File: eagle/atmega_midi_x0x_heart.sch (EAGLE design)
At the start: 39 parts, among them J11_VCF_CUTOFF 22-23-2021, U1 ATMEGA328P_PDIP, U2 TLV2372IP

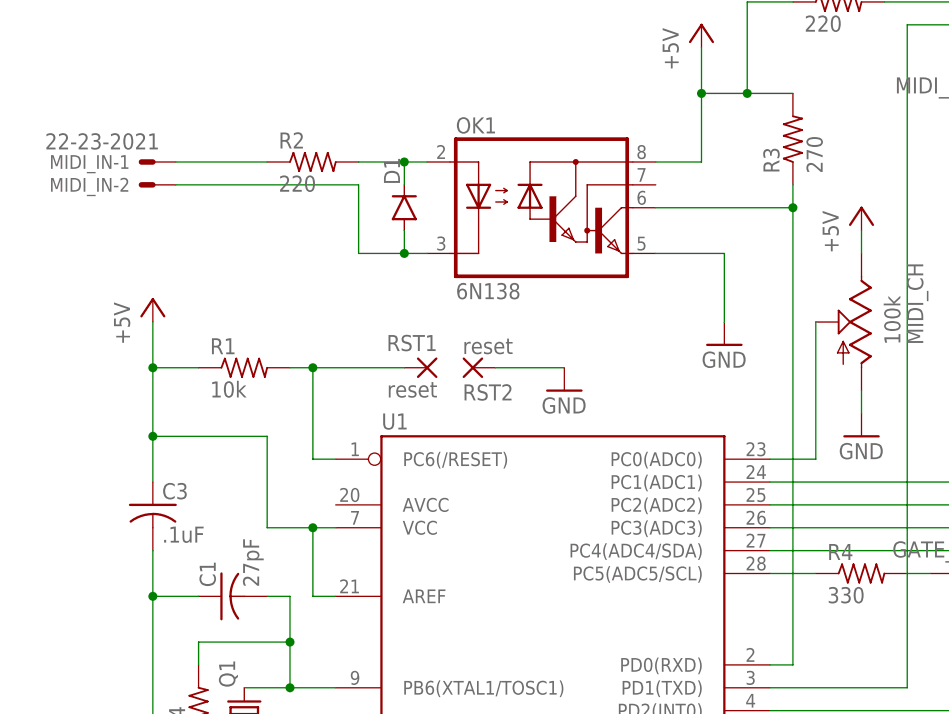
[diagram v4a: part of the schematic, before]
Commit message: initial layout for res control version
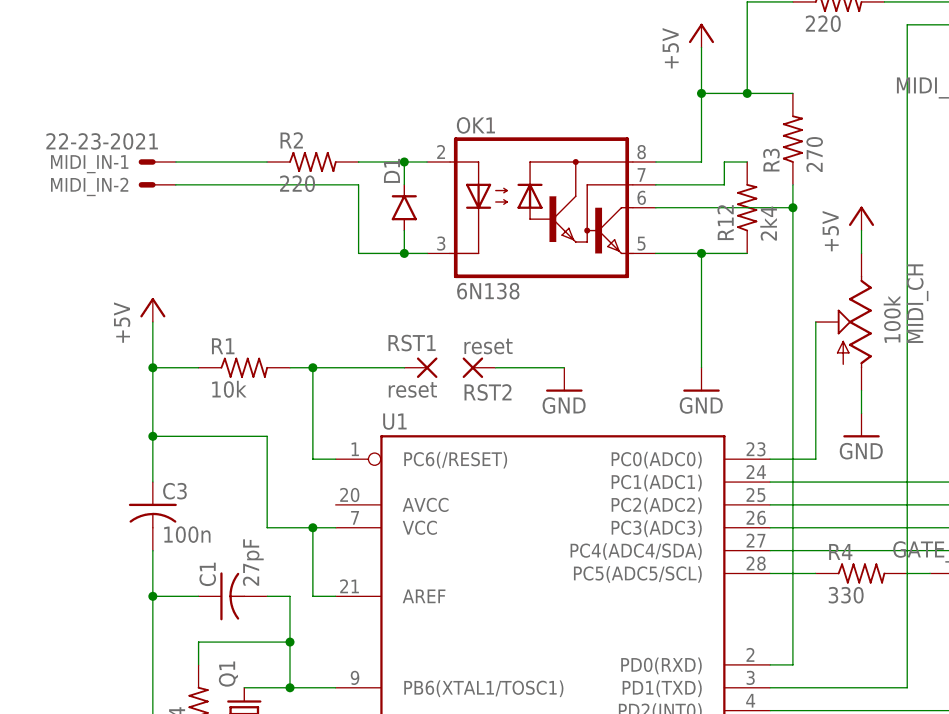
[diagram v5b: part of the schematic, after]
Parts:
- added R12: 2k4, rcl:R-US_0207/10
- C3: value .1uF -> 100n
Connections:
- new net N$44: OK1.VB, R12.2
- net GND: now also R12.1
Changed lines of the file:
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@@
 <part name="R1" library="rcl" deviceset="R-US_" device="0207/10" value="10k"/>
 <part name="OK1" library="optocoupler" deviceset="6N138" device=""/>
-<part name="C3" library="rcl" deviceset="C-US" device="050-024X044" value=".1uF"/>
+<part name="C3" library="rcl" deviceset="C-US" device="050-024X044" value="100n"/>
 <part name="D1" library="SparkFun-DiscreteSemi" deviceset="DIODE" device="1N4148"/>
 <part name="R2" library="rcl" deviceset="R-US_" device="0207/10" value="220"/>
@@
 <part name="MIDI_OUT_THRU" library="con-lstb" deviceset="MA03-1" device=""/>
 <part name="GND15" library="supply1" deviceset="GND" device=""/>
+<part name="R12" library="rcl" deviceset="R-US_" device="0207/10" value="2k4"/>
 </parts>
 <sheets>
@@
 <instance part="GND1" gate="1" x="-25.4" y="10.16"/>
 <instance part="GND2" gate="1" x="20.32" y="81.28"/>
-<instance part="GND3" gate="1" x="38.1" y="86.36"/>
+<instance part="GND3" gate="1" x="35.56" y="81.28"/>
 <instance part="GND4" gate="1" x="73.66" y="78.74"/>
 <instance part="GND5" gate="1" x="53.34" y="76.2"/>
@@
 <instance part="MIDI_OUT_THRU" gate="G$1" x="73.66" y="121.92" rot="R180"/>
 <instance part="GND15" gate="1" x="66.04" y="111.76"/>
+<instance part="R12" gate="G$1" x="40.64" y="101.6" rot="R90"/>
 </instances>
 <busses>
@@
 </segment>
 <segment>
-<wire x1="38.1" y1="96.52" x2="38.1" y2="88.9" width="0.1524" layer="91"/>
+<wire x1="35.56" y1="96.52" x2="35.56" y2="83.82" width="0.1524" layer="91"/>
 <pinref part="OK1" gate="G$1" pin="GND"/>
-<wire x1="30.48" y1="96.52" x2="38.1" y2="96.52" width="0.1524" layer="91"/>
+<wire x1="30.48" y1="96.52" x2="35.56" y2="96.52" width="0.1524" layer="91"/>
 <pinref part="GND3" gate="1" pin="GND"/>
+<pinref part="R12" gate="G$1" pin="1"/>
+<wire x1="40.64" y1="96.52" x2="35.56" y2="96.52" width="0.1524" layer="91"/>
+<junction x="35.56" y="96.52"/>
 </segment>
 <segment>
@@
 </segment>
 </net>
+<net name="N$44" class="0">
+<segment>
+<pinref part="OK1" gate="G$1" pin="VB"/>
+<wire x1="30.48" y1="104.14" x2="38.1" y2="104.14" width="0.1524" layer="91"/>
+<wire x1="38.1" y1="104.14" x2="38.1" y2="106.68" width="0.1524" layer="91"/>
+<pinref part="R12" gate="G$1" pin="2"/>
+<wire x1="38.1" y1="106.68" x2="40.64" y2="106.68" width="0.1524" layer="91"/>
+</segment>
+</net>

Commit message: layout tweaks
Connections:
- net N$37: now also U$1.SCK; no longer U$1.SI
- net N$41: now also U$1.SI; no longer U$1.SCK
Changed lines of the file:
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@@
 <net name="N$41" class="0">
 <segment>
-<wire x1="144.78" y1="43.18" x2="144.78" y2="33.02" width="0.1524" layer="91"/>
-<pinref part="U$1" gate="A" pin="SCK"/>
-<wire x1="144.78" y1="33.02" x2="157.48" y2="33.02" width="0.1524" layer="91"/>
+<wire x1="144.78" y1="43.18" x2="144.78" y2="30.48" width="0.1524" layer="91"/>
 <pinref part="U1" gate="G$1" pin="PD7(AIN1)"/>
 <wire x1="43.18" y1="33.02" x2="78.74" y2="33.02" width="0.1524" layer="91"/>
 <wire x1="78.74" y1="33.02" x2="78.74" y2="43.18" width="0.1524" layer="91"/>
 <wire x1="78.74" y1="43.18" x2="144.78" y2="43.18" width="0.1524" layer="91"/>
+<pinref part="U$1" gate="A" pin="SI"/>
+<wire x1="144.78" y1="30.48" x2="157.48" y2="30.48" width="0.1524" layer="91"/>
 </segment>
 </net>
@@
 <wire x1="81.28" y1="27.94" x2="81.28" y2="40.64" width="0.1524" layer="91"/>
 <wire x1="81.28" y1="40.64" x2="142.24" y2="40.64" width="0.1524" layer="91"/>
-<wire x1="142.24" y1="40.64" x2="142.24" y2="30.48" width="0.1524" layer="91"/>
-<pinref part="U$1" gate="A" pin="SI"/>
-<wire x1="142.24" y1="30.48" x2="157.48" y2="30.48" width="0.1524" layer="91"/>
+<wire x1="142.24" y1="40.64" x2="142.24" y2="33.02" width="0.1524" layer="91"/>
 <pinref part="U1" gate="G$1" pin="PB0(ICP)"/>
 <wire x1="43.18" y1="27.94" x2="81.28" y2="27.94" width="0.1524" layer="91"/>
+<pinref part="U$1" gate="A" pin="SCK"/>
+<wire x1="157.48" y1="33.02" x2="142.24" y2="33.02" width="0.1524" layer="91"/>
 </segment>
 </net>

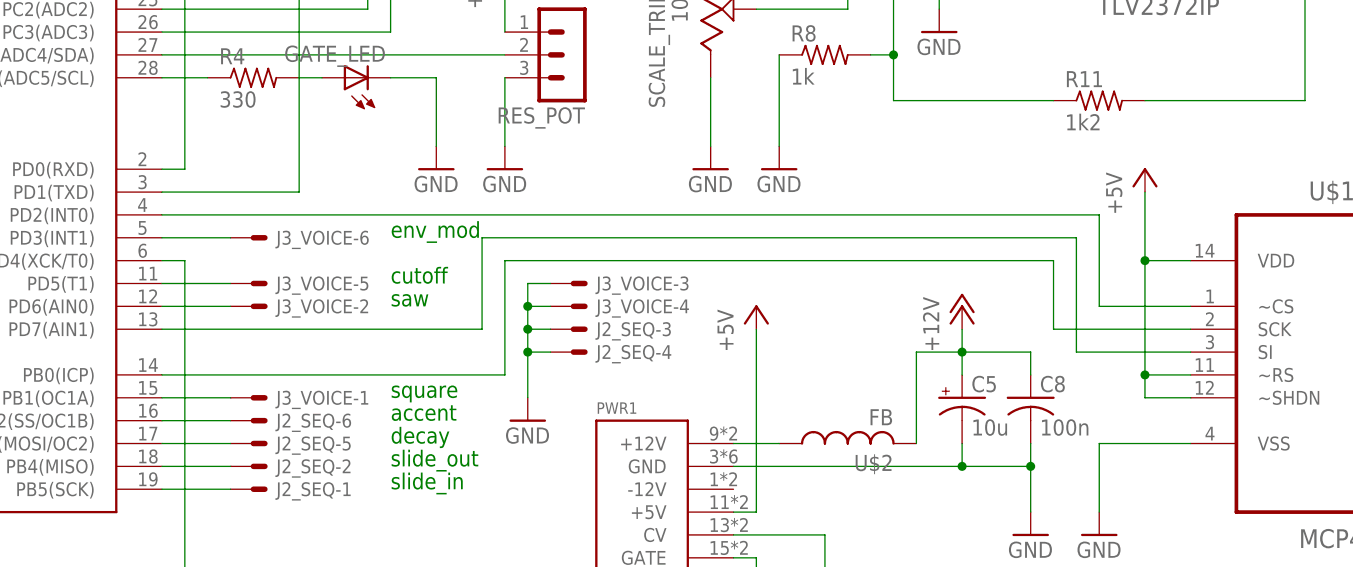
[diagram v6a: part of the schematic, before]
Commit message: 97 pct autorouted
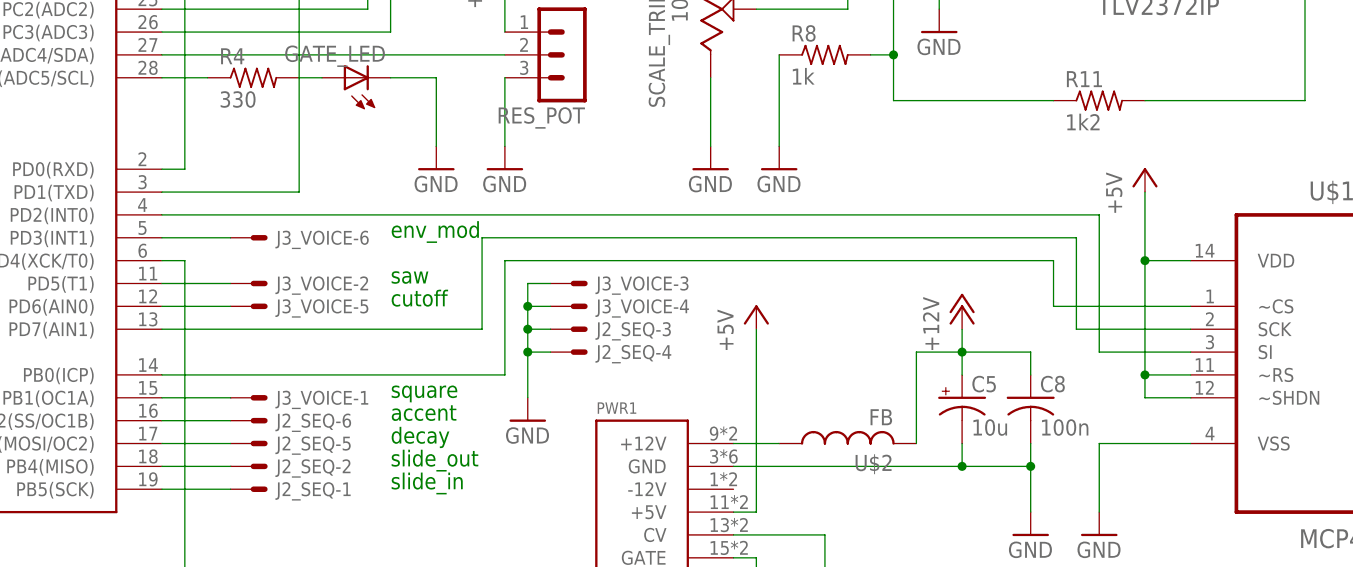
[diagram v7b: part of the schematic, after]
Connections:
- net N$10: now also U1.PD5(T1); no longer U1.PD6(AIN0)
- net N$16: now also U1.PD6(AIN0); no longer U1.PD5(T1)
- net N$37: now also U$1.~CS; no longer U$1.SCK
- net N$40: now also U$1.SI; no longer U$1.~CS
- net N$41: now also U$1.SCK; no longer U$1.SI
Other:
- moved on the sheet: J3_VOICE-2, J3_VOICE-5
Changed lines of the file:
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@@
 <plain>
 <text x="68.58" y="25.4" size="1.778" layer="91">square</text>
-<text x="68.58" y="35.56" size="1.778" layer="91">saw</text>
-<text x="68.58" y="38.1" size="1.778" layer="91">cutoff</text>
+<text x="68.58" y="38.1" size="1.778" layer="91">saw</text>
+<text x="68.58" y="35.56" size="1.778" layer="91">cutoff</text>
 <text x="68.58" y="43.18" size="1.778" layer="91">env_mod</text>
 <text x="68.58" y="15.24" size="1.778" layer="91">slide_in</text>
@@
 <instance part="J11_VCF_CUTOFF" gate="-2" x="187.96" y="76.2"/>
 <instance part="J3_VOICE" gate="-1" x="53.34" y="25.4"/>
-<instance part="J3_VOICE" gate="-2" x="53.34" y="35.56"/>
+<instance part="J3_VOICE" gate="-2" x="53.34" y="38.1"/>
 <instance part="J3_VOICE" gate="-3" x="88.9" y="38.1"/>
 <instance part="J3_VOICE" gate="-4" x="88.9" y="35.56"/>
-<instance part="J3_VOICE" gate="-5" x="53.34" y="38.1"/>
+<instance part="J3_VOICE" gate="-5" x="53.34" y="35.56"/>
 <instance part="J3_VOICE" gate="-6" x="53.34" y="43.18"/>
 <instance part="J2_SEQ" gate="-1" x="53.34" y="15.24"/>
@@
 </segment>
 </net>
-<net name="N$10" class="0">
-<segment>
-<pinref part="J3_VOICE" gate="-2" pin="S"/>
-<pinref part="U1" gate="G$1" pin="PD6(AIN0)"/>
-<wire x1="50.8" y1="35.56" x2="43.18" y2="35.56" width="0.1524" layer="91"/>
-</segment>
-</net>
-<net name="N$16" class="0">
-<segment>
-<pinref part="U1" gate="G$1" pin="PD5(T1)"/>
-<pinref part="J3_VOICE" gate="-5" pin="S"/>
-<wire x1="43.18" y1="38.1" x2="50.8" y2="38.1" width="0.1524" layer="91"/>
-</segment>
-</net>
 <net name="GND" class="0">
 <segment>
@@
 <net name="N$40" class="0">
 <segment>
-<pinref part="U$1" gate="A" pin="~CS"/>
-<wire x1="157.48" y1="35.56" x2="147.32" y2="35.56" width="0.1524" layer="91"/>
-<wire x1="147.32" y1="35.56" x2="147.32" y2="45.72" width="0.1524" layer="91"/>
+<wire x1="147.32" y1="30.48" x2="147.32" y2="45.72" width="0.1524" layer="91"/>
 <wire x1="147.32" y1="45.72" x2="43.18" y2="45.72" width="0.1524" layer="91"/>
 <pinref part="U1" gate="G$1" pin="PD2(INT0)"/>
+<pinref part="U$1" gate="A" pin="SI"/>
+<wire x1="147.32" y1="30.48" x2="157.48" y2="30.48" width="0.1524" layer="91"/>
 </segment>
 </net>
 <net name="N$41" class="0">
 <segment>
-<wire x1="144.78" y1="43.18" x2="144.78" y2="30.48" width="0.1524" layer="91"/>
+<wire x1="144.78" y1="43.18" x2="144.78" y2="33.02" width="0.1524" layer="91"/>
 <pinref part="U1" gate="G$1" pin="PD7(AIN1)"/>
 <wire x1="43.18" y1="33.02" x2="78.74" y2="33.02" width="0.1524" layer="91"/>
 <wire x1="78.74" y1="33.02" x2="78.74" y2="43.18" width="0.1524" layer="91"/>
 <wire x1="78.74" y1="43.18" x2="144.78" y2="43.18" width="0.1524" layer="91"/>
-<pinref part="U$1" gate="A" pin="SI"/>
-<wire x1="144.78" y1="30.48" x2="157.48" y2="30.48" width="0.1524" layer="91"/>
+<pinref part="U$1" gate="A" pin="SCK"/>
+<wire x1="157.48" y1="33.02" x2="144.78" y2="33.02" width="0.1524" layer="91"/>
 </segment>
 </net>
@@
 <wire x1="81.28" y1="27.94" x2="81.28" y2="40.64" width="0.1524" layer="91"/>
 <wire x1="81.28" y1="40.64" x2="142.24" y2="40.64" width="0.1524" layer="91"/>
-<wire x1="142.24" y1="40.64" x2="142.24" y2="33.02" width="0.1524" layer="91"/>
+<wire x1="142.24" y1="40.64" x2="142.24" y2="35.56" width="0.1524" layer="91"/>
 <pinref part="U1" gate="G$1" pin="PB0(ICP)"/>
 <wire x1="43.18" y1="27.94" x2="81.28" y2="27.94" width="0.1524" layer="91"/>
-<pinref part="U$1" gate="A" pin="SCK"/>
-<wire x1="157.48" y1="33.02" x2="142.24" y2="33.02" width="0.1524" layer="91"/>
+<pinref part="U$1" gate="A" pin="~CS"/>
+<wire x1="157.48" y1="35.56" x2="142.24" y2="35.56" width="0.1524" layer="91"/>
 </segment>
 </net>
@@
 </segment>
 </net>
+<net name="N$10" class="0">
+<segment>
+<pinref part="J3_VOICE" gate="-2" pin="S"/>
+<pinref part="U1" gate="G$1" pin="PD5(T1)"/>
+<wire x1="50.8" y1="38.1" x2="43.18" y2="38.1" width="0.1524" layer="91"/>
+</segment>
+</net>
+<net name="N$16" class="0">
+<segment>
+<pinref part="U1" gate="G$1" pin="PD6(AIN0)"/>
+<pinref part="J3_VOICE" gate="-5" pin="S"/>
+<wire x1="43.18" y1="35.56" x2="50.8" y2="35.56" width="0.1524" layer="91"/>
+</segment>
+</net>

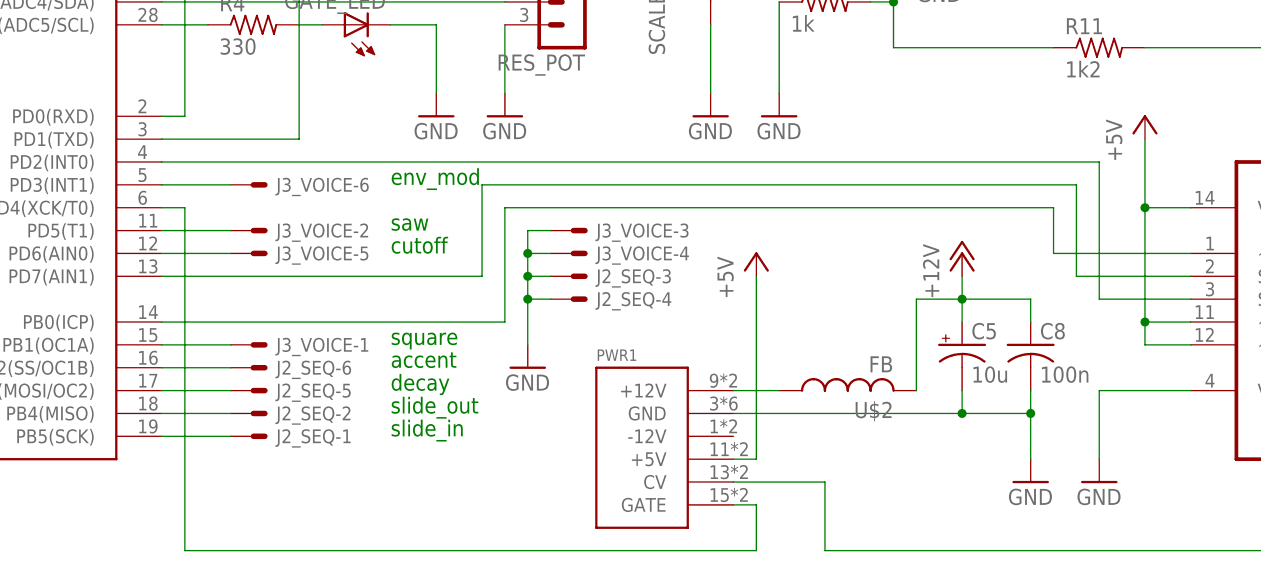
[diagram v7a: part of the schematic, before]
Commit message: switched gate and pot ctrl pins for positioning
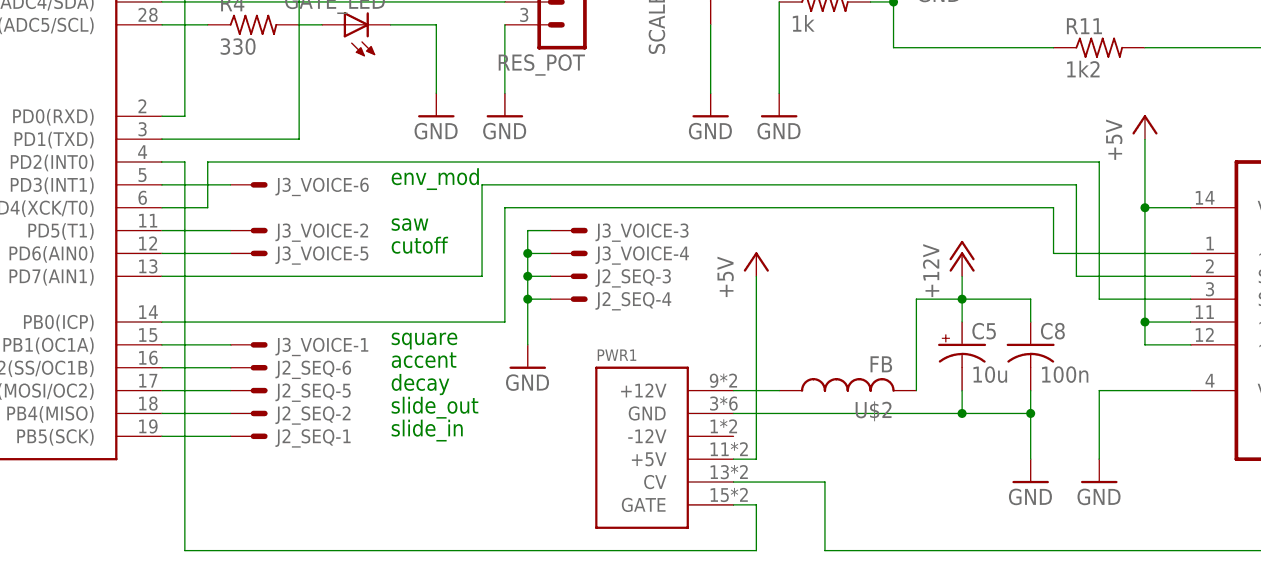
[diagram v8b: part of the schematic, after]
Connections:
- net N$22: now also U$1.SI; no longer PWR1.GATE
- net N$40: now also PWR1.GATE; no longer U$1.SI
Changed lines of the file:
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@@
 <net name="N$22" class="0">
 <segment>
-<wire x1="45.72" y1="40.64" x2="45.72" y2="2.54" width="0.1524" layer="91"/>
-<wire x1="45.72" y1="40.64" x2="43.18" y2="40.64" width="0.1524" layer="91"/>
+<wire x1="147.32" y1="30.48" x2="147.32" y2="45.72" width="0.1524" layer="91"/>
+<wire x1="147.32" y1="45.72" x2="48.26" y2="45.72" width="0.1524" layer="91"/>
+<pinref part="U$1" gate="A" pin="SI"/>
+<wire x1="147.32" y1="30.48" x2="157.48" y2="30.48" width="0.1524" layer="91"/>
+<wire x1="48.26" y1="45.72" x2="48.26" y2="40.64" width="0.1524" layer="91"/>
 <pinref part="U1" gate="G$1" pin="PD4(XCK/T0)"/>
-<pinref part="PWR1" gate="G$1" pin="GATE"/>
-<wire x1="109.22" y1="7.62" x2="106.68" y2="7.62" width="0.1524" layer="91"/>
-<wire x1="109.22" y1="2.54" x2="109.22" y2="7.62" width="0.1524" layer="91"/>
-<wire x1="45.72" y1="2.54" x2="109.22" y2="2.54" width="0.1524" layer="91"/>
+<wire x1="48.26" y1="40.64" x2="43.18" y2="40.64" width="0.1524" layer="91"/>
 </segment>
 </net>
@@
 </segment>
 </net>
-<net name="N$40" class="0">
-<segment>
-<wire x1="147.32" y1="30.48" x2="147.32" y2="45.72" width="0.1524" layer="91"/>
-<wire x1="147.32" y1="45.72" x2="43.18" y2="45.72" width="0.1524" layer="91"/>
-<pinref part="U1" gate="G$1" pin="PD2(INT0)"/>
-<pinref part="U$1" gate="A" pin="SI"/>
-<wire x1="147.32" y1="30.48" x2="157.48" y2="30.48" width="0.1524" layer="91"/>
-</segment>
-</net>
 <net name="N$41" class="0">
 <segment>
@@
 </segment>
 </net>
+<net name="N$40" class="0">
+<segment>
+<pinref part="PWR1" gate="G$1" pin="GATE"/>
+<wire x1="109.22" y1="7.62" x2="106.68" y2="7.62" width="0.1524" layer="91"/>
+<wire x1="109.22" y1="2.54" x2="109.22" y2="7.62" width="0.1524" layer="91"/>
+<pinref part="U1" gate="G$1" pin="PD2(INT0)"/>
+<wire x1="45.72" y1="45.72" x2="43.18" y2="45.72" width="0.1524" layer="91"/>
+<wire x1="45.72" y1="45.72" x2="45.72" y2="2.54" width="0.1524" layer="91"/>
+<wire x1="45.72" y1="2.54" x2="109.22" y2="2.54" width="0.1524" layer="91"/>
+</segment>
+</net>
